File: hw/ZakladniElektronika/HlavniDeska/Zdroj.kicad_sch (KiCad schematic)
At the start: 24 parts, among them Q3 Q_PMOS_DGS, Q4 Q_NMOS_DGS, Q5 Q_PMOS_DGS, Q6 Q_NMOS_DGS, U33 Polyfuse, U34 Polyfuse

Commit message: WIP
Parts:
- removed D124: D_Schottky, Diode_SMD:D_SOD-123F, symbol Device:D_Schottky
- removed TP1, TP2, TP3: TP_06MM, RBCX:TP_06MM, symbol RBCX-eagle-import:TP_06MM
- removed U33, U34: Polyfuse, Inductor_SMD:L_1206_3216Metric, symbol B.B-rescue:Polyfuse-Device-B.B-rescue-B.B-rescue
- added F1, F2: Polyfuse, Inductor_SMD:L_1206_3216Metric, symbol Device:Polyfuse
- added TP1, TP2, TP3: Conn_01x01, Connector_Pin:Pin_D0.7mm_L6.5mm_W1.8mm_FlatFork, symbol Connector_Generic:Conn_01x01
- C143: Basic/Extended E -> B; LCSC C131394 -> C307331; info (none) -> 50V, X7R
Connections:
- net BAT+: now also TP2.1 (Pin_1)
- net at C144.1, Q6.2 (G), R18.1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: now also TP3.1 (Pin_1)
- net at Q5.2 (G), R16.2, R17.2: now also TP1.1 (Pin_1)
- net at Q3.1 (D): now also F1.1, F2.1
- net at BT2.1 (+): now also F1.2
- net at BT1.1 (+): now also F2.2
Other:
- moved on the sheet: BT1, BT2, Q4, R1, R14, R2

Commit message: Zaciame psat
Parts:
- removed C143: 100n, Capacitor_SMD:C_0402_1005Metric, symbol Device:C
- removed C144: 2.2u, Capacitor_SMD:C_0402_1005Metric, symbol Device:C
- removed C145: C_Polarized, Capacitor_SMD:CP_Elec_8x11.9, symbol Device:C_Polarized
- removed Q3, Q5: Q_PMOS_DGS, RBCX:JMSL0302AU, symbol Device:Q_PMOS_DGS
- removed Q4, Q6: Q_NMOS_DGS, Package_TO_SOT_SMD:SOT-723, symbol Device:Q_NMOS_DGS
- removed R1, R17, R19, R2: 10k, Capacitor_SMD:C_0201_0603Metric, symbol Device:R
- removed R14, R20: 330, Capacitor_SMD:C_0201_0603Metric, symbol Device:R
- removed R15, R16: 100k, Capacitor_SMD:C_0201_0603Metric, symbol Device:R
- removed R18: 1M, Resistor_SMD:R_0201_0603Metric, symbol Device:R
- removed TP1, TP2, TP3: Conn_01x01, Connector_Pin:Pin_D0.7mm_L6.5mm_W1.8mm_FlatFork, symbol Connector_Generic:Conn_01x01
- added C138: 1u, Resistor_SMD:R_0402_1005Metric, symbol Device:C
- added Q? (x3): Q_NMOS_DGS, symbol Device:Q_NMOS_DGS
- added R23 (x3): 200, Resistor_SMD:R_0402_1005Metric, symbol Device:R
- added U3: BQ298012, symbol Robotarna_KiCad_Library:BQ298xyz
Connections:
- net GND: now also C138.2, Q?.1 (D), U3.3 (GND), U3.4 (CS); no longer BT1.2 (-), BT2.2 (-)
- net VCC: now also Q?.3 (S), R23.1
- net at BT2.1 (+): now also F2.2; no longer F1.2
- net at F1.1, F2.1: now also Q?.2 (G), Q?.3 (S), R23.1, R23.1
- net at BT1.1 (+): now also F1.2; no longer F2.2
- new net: C138.1, R23.2, U3.2 (VDD)
- new net: Q?.1 (D), Q?.1 (D)
- new net: Q?.2 (G), U3.7 (DSG)
- new net: BT1.2 (-), BT2.2 (-), Q?.3 (S)
- new net: R23.2, U3.6 (PACK)
- new net: Q?.2 (G), U3.8 (CHG)
- new net: R23.2, U3.1 (BAT)
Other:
- note added: "N-MOS -> C2926777 -> C141589"
- note removed: "Ochrana gatu Q3 proti napětovím špičkám na napájení - společně s kapacitou gatu tvoří filtr typu DP"

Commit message: Zavazbení zapínání
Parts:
- removed Q? (x2): Q_NMOS_DGS, symbol Device:Q_NMOS_DGS
- added C138 (x2): 1u, Resistor_SMD:R_0402_1005Metric, symbol Device:C
- added Q? (x2): Q_NMOS_DGS, symbol Device:Q_NMOS_DGS
- added Q? (x3): Q_NMOS_DGS, Package_TO_SOT_SMD:SOT-23, symbol Device:Q_NMOS_DGS
- added R13 (x2): 10k, Resistor_SMD:R_0402_1005Metric, symbol Device:R
- added R13: 200k, Resistor_SMD:R_0402_1005Metric, symbol Device:R
- added R13 (x2): 1M, Resistor_SMD:R_0402_1005Metric, symbol Device:R
- added R23: 200, Resistor_SMD:R_0402_1005Metric, symbol Device:R
- added TP1: TestPoint-Q16_G, symbol Connector:TestPoint
- added TP2: TestPoint-BAT, symbol Connector:TestPoint
- added TP3: TestPoint-VCC, symbol Connector:TestPoint
- added TP4: TestPoint-BUTTON_ON, symbol Connector:TestPoint
- added TP5: TestPoint-EN_ALL, symbol Connector:TestPoint
- Q?: Basic/Extended (none) -> E; LCSC (none) -> C2926777
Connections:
- net BUTTON_ON: now also Q?.1 (D), R13.1
- net GND: now also Q?.3 (S), C138.2, Q?.3 (S), Q?.3 (S), Q?.3 (S), R13.1; no longer Q?.1 (D)
- net ON: now also C138.2, Q?.2 (G), R13.1, TP4.1
- net VCC: now also Q?.3 (S), TP3.1
- net at F1.1, F2.1, Q?.2 (G)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: now also Q?.3 (S), R13.2, TP2.1
- net at U3.7 (DSG): now also Q?.2 (G)
- net at BT1.2 (-), BT2.2 (-): now also Q?.1 (D); no longer Q?.3 (S)
- net at U3.8 (CHG): now also Q?.2 (G)
- net at U3.5 (CTR): now also Q?.1 (D)
- new net: Q?.1 (D), Q?.1 (D)
- new net: C138.1, Q?.2 (G), R13.1, R13.2, R23.1, TP5.1
- new net: C138.1, Q?.1 (D), Q?.2 (G), R13.1, R13.2, TP1.1
- new net EN_ALL: R23.2
- new net IO_VCC: R13.2, R13.2
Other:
- moved on the sheet: BT1, BT2, F1, F2, Q?, R23

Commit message: USB_multiplexer a přehlednost
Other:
- note removed: "N-MOS -> C2926777 -> C141589"
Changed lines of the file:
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@@
     (effects (font (size 1.5 1.5) (thickness 0.3) bold) (justify left bottom))
-  )
-  (text "N-MOS -> C2926777\n	  -> C141589" (at 46.99 54.61 0)
-    (effects (font (size 1.27 1.27)) (justify left bottom))
   )
   (label "VCC" (at 236.22 50.8 0) (fields_autoplaced)
     (effects (font (size 1.27 1.27)) (justify left bottom))
   )
-  (hierarchical_label "GND" (shape input) (at 190.5 137.16 270) (fields_autoplaced)
-    (effects (font (size 1.27 1.27)) (justify right))
-  )
-  (hierarchical_label "GND" (shape input) (at 114.3 137.16 270) (fields_autoplaced)
+  (hierarchical_label "GND" (shape passive) (at 124.46 73.66 270) (fields_autoplaced)
     (effects (font (size 1.27 1.27)) (justify right))
   )
@@
     (effects (font (size 1.27 1.27)) (justify left))
   )
-  (hierarchical_label "GND" (shape input) (at 177.8 106.68 270) (fields_autoplaced)
-    (effects (font (size 1.27 1.27)) (justify right))
-  )
-  (hierarchical_label "GND" (shape input) (at 177.8 137.16 270) (fields_autoplaced)
+  (hierarchical_label "GND" (shape passive) (at 203.2 77.47 270) (fields_autoplaced)
+    (effects (font (size 1.27 1.27)) (justify right))
+  )
+  (hierarchical_label "GND" (shape passive) (at 165.1 73.66 270) (fields_autoplaced)
+    (effects (font (size 1.27 1.27)) (justify right))
+  )
+  (hierarchical_label "GND" (shape passive) (at 177.8 137.16 270) (fields_autoplaced)
+    (effects (font (size 1.27 1.27)) (justify right))
+  )
+  (hierarchical_label "GND" (shape passive) (at 152.4 137.16 270) (fields_autoplaced)
     (effects (font (size 1.27 1.27)) (justify right))
   )
@@
     (effects (font (size 1.27 1.27)) (justify left))
   )
-  (hierarchical_label "GND" (shape input) (at 165.1 73.66 270) (fields_autoplaced)
-    (effects (font (size 1.27 1.27)) (justify right))
-  )
-  (hierarchical_label "GND" (shape input) (at 190.5 77.47 270) (fields_autoplaced)
+  (hierarchical_label "GND" (shape passive) (at 177.8 106.68 270) (fields_autoplaced)
+    (effects (font (size 1.27 1.27)) (justify right))
+  )
+  (hierarchical_label "GND" (shape passive) (at 190.5 137.16 270) (fields_autoplaced)
     (effects (font (size 1.27 1.27)) (justify right))
   )
@@
     (effects (font (size 1.27 1.27)) (justify left))
   )
+  (hierarchical_label "GND" (shape passive) (at 114.3 137.16 270) (fields_autoplaced)
+    (effects (font (size 1.27 1.27)) (justify right))
+  )
+  (hierarchical_label "GND" (shape passive) (at 190.5 77.47 270) (fields_autoplaced)
+    (effects (font (size 1.27 1.27)) (justify right))
+  )
   (hierarchical_label "ON" (shape input) (at 137.16 114.3 180) (fields_autoplaced)
     (effects (font (size 1.27 1.27)) (justify right))
   )
   (hierarchical_label "BUTTON_ON" (shape output) (at 111.76 119.38 180) (fields_autoplaced)
-    (effects (font (size 1.27 1.27)) (justify right))
-  )
-  (hierarchical_label "GND" (shape input) (at 203.2 77.47 270) (fields_autoplaced)
-    (effects (font (size 1.27 1.27)) (justify right))
-  )
-  (hierarchical_label "GND" (shape input) (at 124.46 73.66 270) (fields_autoplaced)
-    (effects (font (size 1.27 1.27)) (justify right))
-  )
-  (hierarchical_label "GND" (shape input) (at 152.4 137.16 270) (fields_autoplaced)
     (effects (font (size 1.27 1.27)) (justify right))
   )
@@
       (effects (font (size 1.27 1.27)) hide)
     )
+    (pin "1")
+    (pin "2")
+    (pin "3")
+    (pin "4")
+    (pin "5")
     (pin "6")
-    (pin "2")
-    (pin "1")
+    (pin "7")
     (pin "8")
-    (pin "4")
-    (pin "3")
-    (pin "5")
-    (pin "7")
-    (instances
-      (project "ZakladniElektronika"
+    (instances
+      (project "ZakladniElektronika"

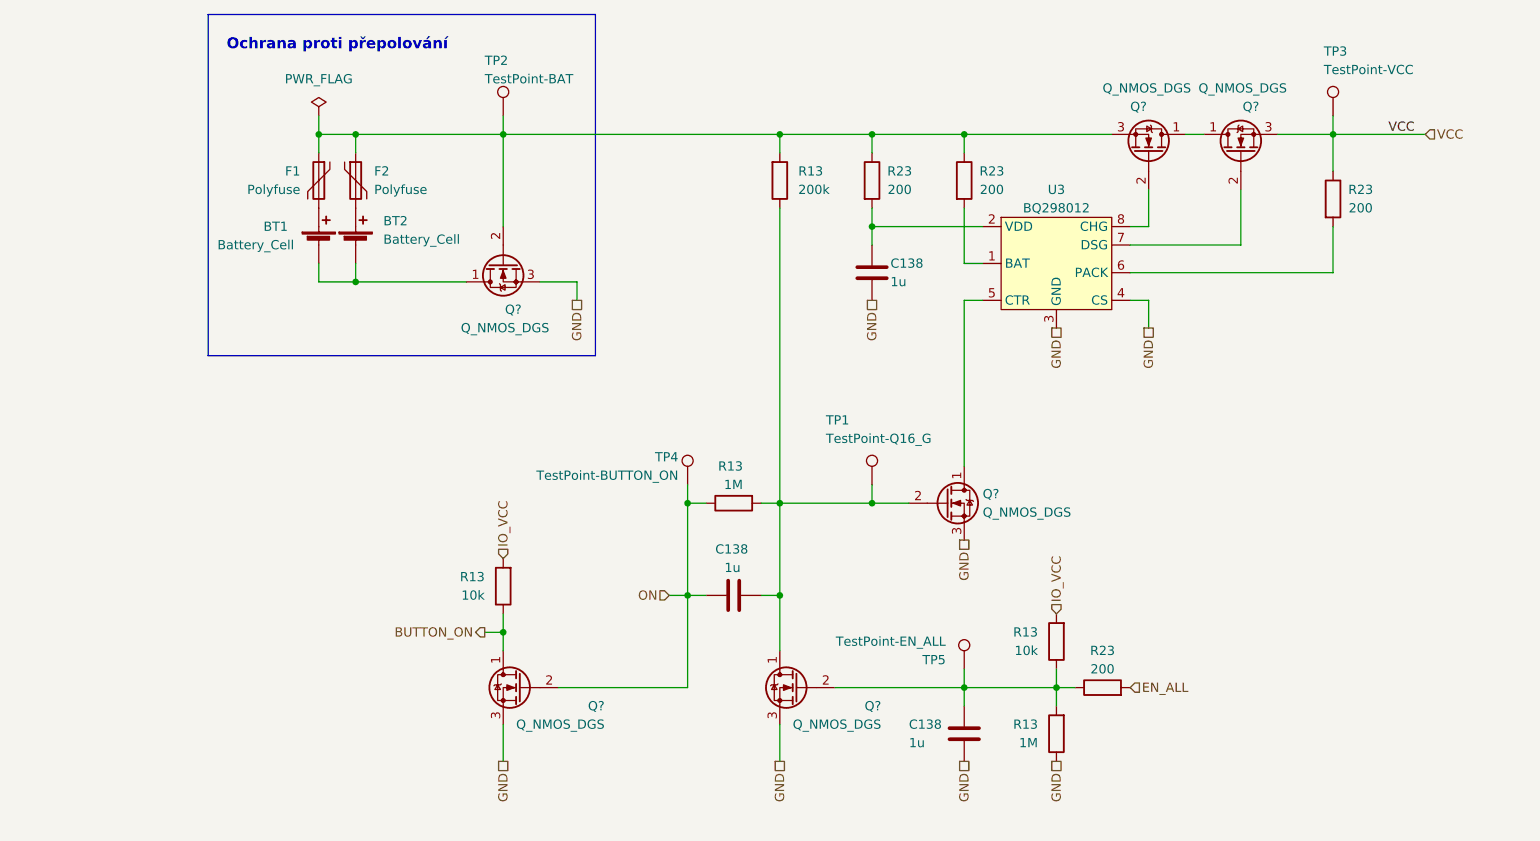
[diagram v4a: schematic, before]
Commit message: Likvidace MiniUI jako samostatné desky a výběr všech komponent
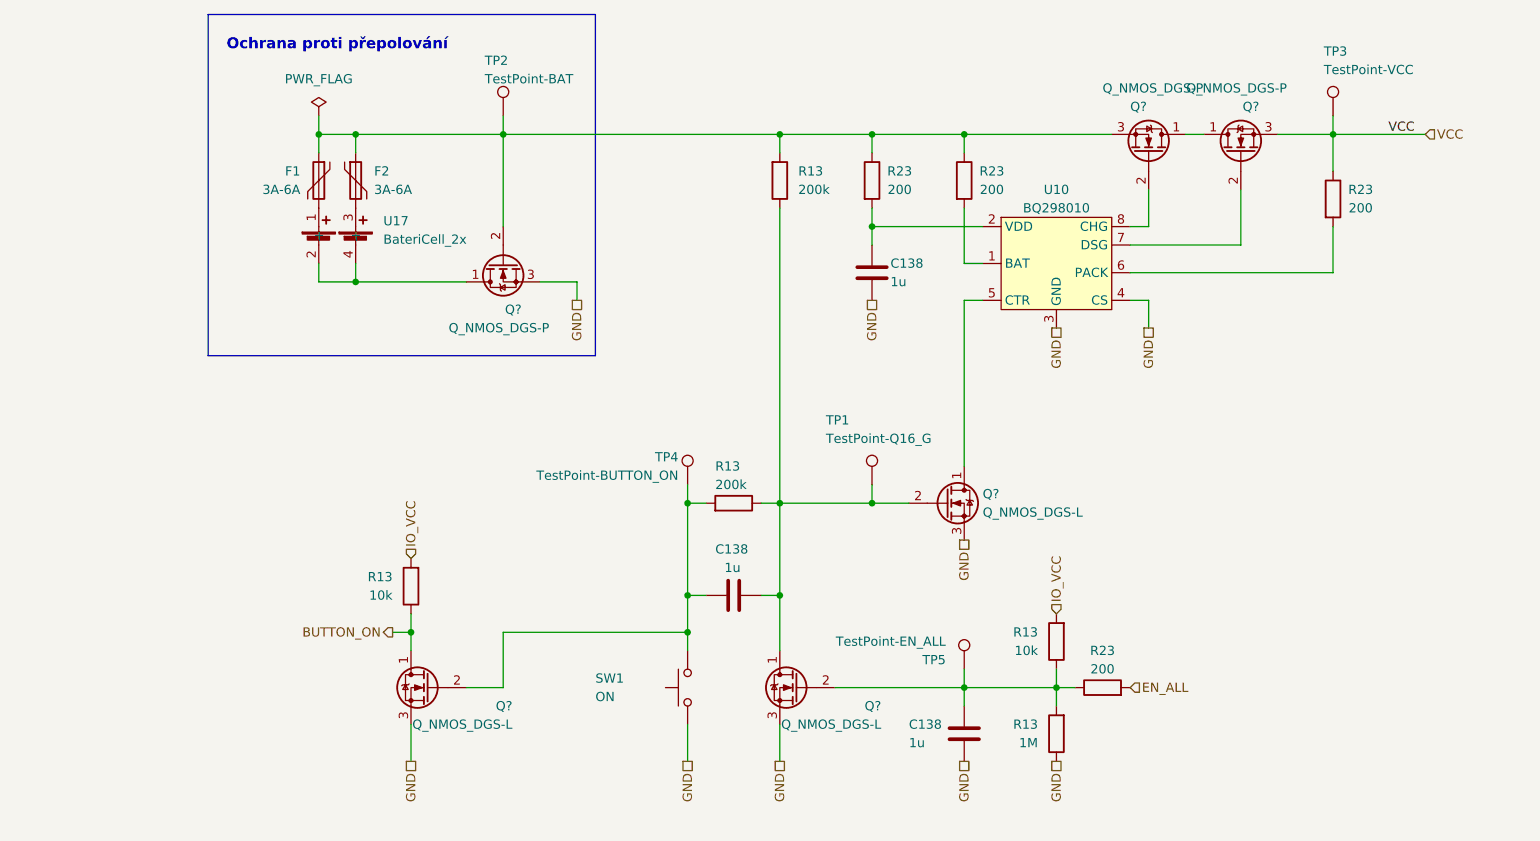
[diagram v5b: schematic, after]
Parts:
- removed BT1, BT2: Battery_Cell, symbol Device:Battery_Cell
- removed U3: BQ298012, symbol Robotarna_KiCad_Library:BQ298xyz
- added SW1: ON, RLK-ElectorMechanicalComponents:TCF2QR, symbol Switch:SW_Push
- added U10: BQ298010, symbol RKL-BatteryManager:BQ298xyz
- added U17: BateriCell_2x, RKL-Batteries:battery_dock, symbol RKL-BatteryManager:BateriCell_2x
- C138: footprint Resistor_SMD:R_0402_1005Metric -> Capacitor_SMD:C_0402_1005Metric; Basic/Extended B -> E; JLCPCB_CORRECTION (none) -> 0;0;0; LCSC C52923 -> C1518208; info (none) -> 50V, X5R (potenciálně C52923 což je 25V, X5R )
- F1, F2: value Polyfuse -> 3A-6A; Basic/Extended (none) -> E; LCSC C20988 -> C883136; info (none) -> 3A hold, 6A trip, 100A max, 6V, 4s, 0,05 Ohm max
- Q? (x3): value Q_NMOS_DGS -> Q_NMOS_DGS-P; footprint (none) -> Package_SON:Diodes_PowerDI3333-8
- Q? (x3): value Q_NMOS_DGS -> Q_NMOS_DGS-L; Basic/Extended E -> B
- R13: JLCPCB_CORRECTION (none) -> 0;0;0
- R13: value 1M -> 200k; LCSC C26083 -> C25764
- R23: Basic/Extended (none) -> B
- TP1, TP2, TP3, TP4, TP5: JLCPCB_IGNORE (none) -> ignore
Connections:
- net GND: now also SW1.1, U10.3 (GND), U10.4 (CS)
- net at Q?.2 (G): now also U10.7 (DSG)
- net at C138.1, R23.2: now also U10.2 (VDD)
- net at F2.2: now also U17.3 (+)
- net at Q?.1 (D): now also U17.2 (-), U17.4 (-)
- net at C138.1, Q?.1 (D), Q?.2 (G)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: now also R13.1; no longer R13.2
- net at Q?.1 (D): now also U10.5 (CTR)
- net at F1.2: now also U17.1 (+)
- net at R23.2: now also U10.6 (PACK)
- net at R23.2: now also U10.1 (BAT)
- net at Q?.2 (G): now also U10.8 (CHG)
- net ON: no longer names the net of C138.2, Q?.2 (G), TP4.1
- net ON: now also R13.2, SW1.2; no longer R13.1
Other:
- moved on the sheet: Q?, R13

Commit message: Výmněna ochrany baterie
Předchozí ochranný čip JLCPCB nemělo na skladě
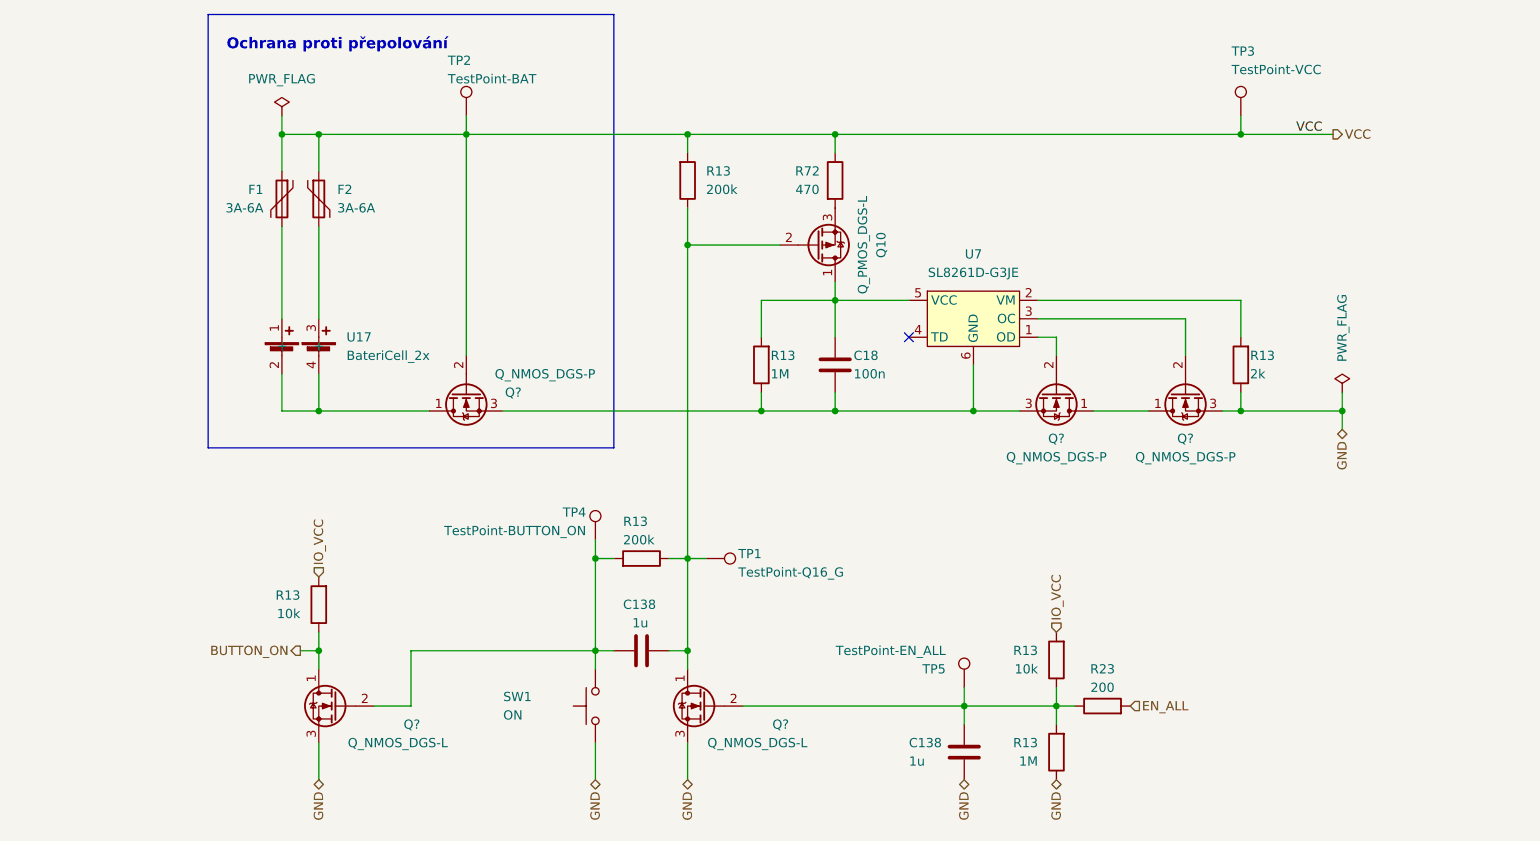
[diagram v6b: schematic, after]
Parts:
- removed C138: 1u, Capacitor_SMD:C_0402_1005Metric, symbol Device:C
- removed Q?: Q_NMOS_DGS-L, Package_TO_SOT_SMD:SOT-23, symbol Device:Q_NMOS_DGS
- removed R13: 200k, Resistor_SMD:R_0402_1005Metric, symbol Device:R
- removed R23 (x3): 200, Resistor_SMD:R_0402_1005Metric, symbol Device:R
- removed U10: BQ298010, symbol RKL-BatteryManager:BQ298xyz
- added C18: 100n, Capacitor_SMD:C_0402_1005Metric, symbol Device:C
- added Q10: Q_PMOS_DGS-L, Package_TO_SOT_SMD:SOT-23, symbol Device:Q_PMOS_DGS
- added R13: 1M, Resistor_SMD:R_0402_1005Metric, symbol Device:R
- added R13: 2k, Resistor_SMD:R_0402_1005Metric, symbol Device:R
- added R13: 200k, Resistor_SMD:R_0402_1005Metric, symbol Device:R
- added R72: 470, Resistor_SMD:R_0402_1005Metric, symbol Device:R
- added U7: SL8261D-G3JE, Package_TO_SOT_SMD:SOT-23-6, symbol RKL-BatteryManager:DW01A
- TP1, TP2, TP3, TP4, TP5: footprint (none) -> Connector_Pin:Pin_D0.9mm_L10.0mm_W2.4mm_FlatFork
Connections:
- net GND: now also Q?.3 (S), R13.1; no longer Q?.3 (S)
- net VCC: now also F1.1, F2.1, Q?.2 (G), TP2.1, R13.2, R72.1; no longer Q?.3 (S)
- net at Q?.2 (G): now also U7.1 (OD)
- net at C138.1, Q?.1 (D), R13.1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: now also Q10.2 (G), R13.1
- net at Q?.2 (G): now also U7.3 (OC)
- new net: C18.2, Q?.3 (S), Q?.3 (S), R13.1, U7.6 (GND)
- new net: C18.1, Q10.1 (D), R13.2, U7.5 (VCC)
- new net: R13.2, U7.2 (VM)
- new net: Q10.3 (S), R72.2
- no-connect marks 0 -> 1
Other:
- moved on the sheet: C138, F1, F2, Q?, R13, R23, SW1, TP1, TP2, TP3, TP4, TP5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
